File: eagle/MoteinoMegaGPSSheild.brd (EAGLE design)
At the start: 58.1 x 33.6 mm, 26 parts, among them J1 BilgeSwitch, J10 LIPO_VCC, J11 LIPO_GND, J2 Button, J3 LED, J4 DS18B20, J5 DS18B20, J6 5V_GND, J7 OKI-78SR-5/1.5, J8 5V, J9 12-24V_VCC, Q1 NDP6020P, Q2 IRF9Z14PBF, Q3 2N7000

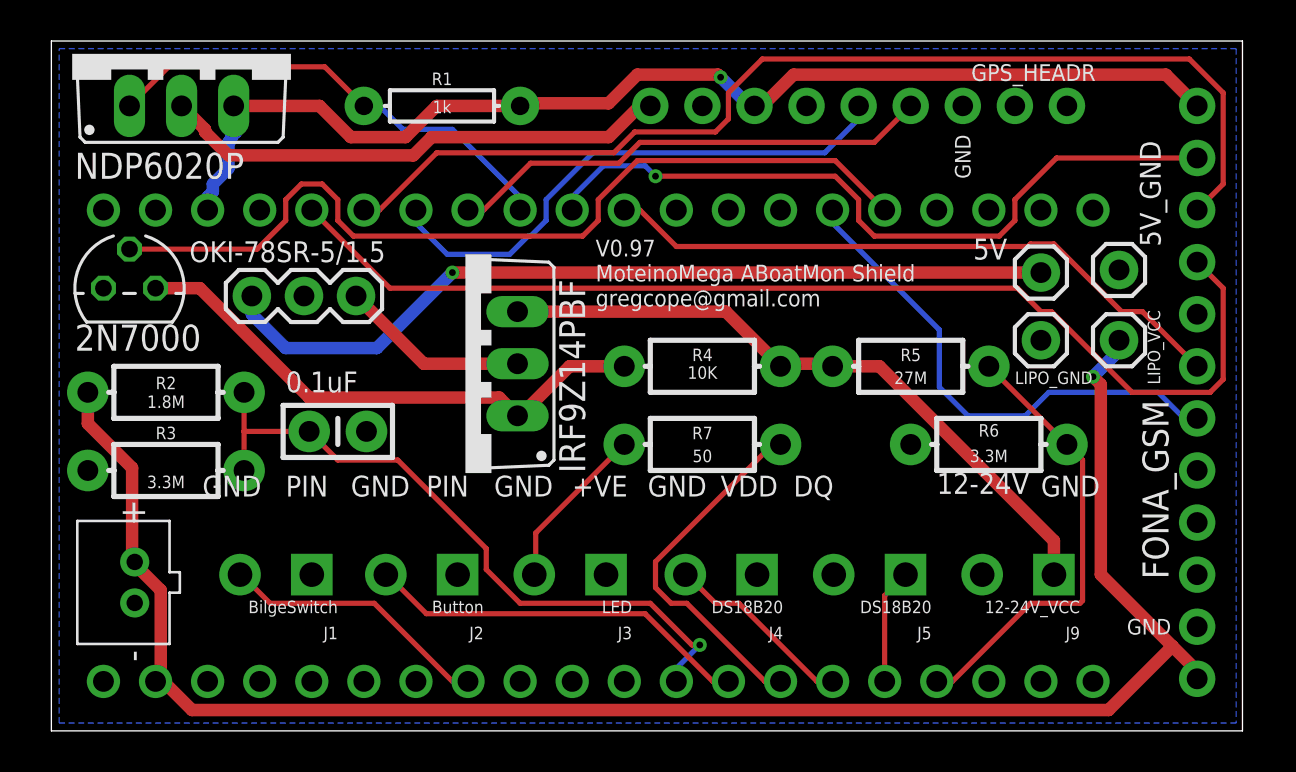
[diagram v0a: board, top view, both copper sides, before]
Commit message: V0.98, schematic layout tweaks, corrected GSM power error, removed GSM power
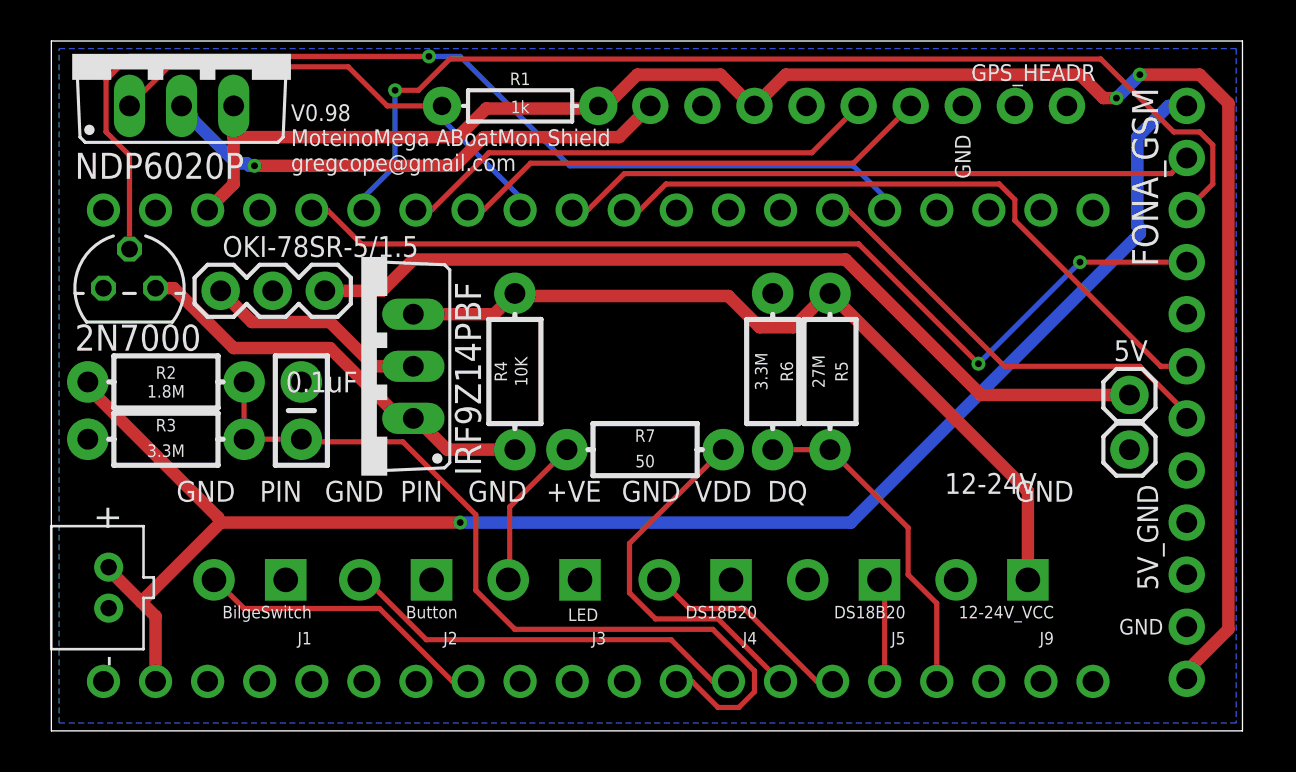
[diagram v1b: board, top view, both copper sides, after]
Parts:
- removed J10: LIPO_VCC, SparkFun-Connectors:1X01
- removed J11: LIPO_GND, SparkFun-Connectors:1X01
- moved R6 11.1 mm to (35.2, 46.7), turned to 270 degrees
- moved R4 9.15 mm to (22.6, 46.7), turned to 90 degrees
- moved J6 8.78 mm to (52.6, 42.9)
- moved J8 7.37 mm to (52.6, 45.6)
- moved Q2 5.08 mm to (15.1, 47.0)
- moved R5 3.95 mm to (38.0, 46.7), turned to 270 degrees
- moved R1 3.81 mm to (22.9, 59.7)
- moved J7 3.57 mm to (13.3, 50.7), turned to 180 degrees
- moved R7 2.81 mm to (29.0, 42.9)
- moved C1 2.05 mm to (12.2, 44.8), turned to 90 degrees
- moved R3 1.52 mm to (5.59, 43.4)
- moved J4 1.30 mm to (33.1, 36.6)
- moved J9 1.30 mm to (47.6, 36.6)
- moved JST1 1.30 mm to (2.79, 36.2)
- moved J1 1.30 mm to (11.4, 36.6)
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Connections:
- net 3.3V: now also JP2.12; no longer JP2.1
- net GND: no longer J11.1
- net VIN: now also JP2.1; no longer J10.1, JP2.12
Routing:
- net 3.3V: track 56.5 -> 87.0 mm, vias 1 -> 2
- net 12-24V-VCC: track 32.5 -> 40.0 mm
- net D19_PWRON: track 43.5 -> 50.7 mm, vias 0 -> 1
- net A0: track 33.2 -> 40.2 mm, vias 1 -> 0
- net D8: track 54.6 -> 47.8 mm, vias 0 -> 2
- net VIN: track 86.3 -> 80.0 mm
- net A5: track 22.1 -> 16.3 mm
- net N$2: track 26.4 -> 20.8 mm
- net D13_NETSTAT: track 35.9 -> 31.0 mm, vias 1 -> 0
- net D18_PS: track 24.9 -> 21.6 mm
- net D10_RX1: track 26.8 -> 23.7 mm
- net 12-24V-SW: track 9.24 -> 10.9 mm
- net D27: track 9.34 -> 10.5 mm
- net D25: track 18.9 -> 20.0 mm
- net D3: track 13.3 -> 14.4 mm
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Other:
- board text added: "V0.98 MoteinoMega ABoatMon Shield gregcope@gmail.com"
- board text removed: "V0.97 MoteinoMega ABoatMon Shield gregcope@gmail.com"

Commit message: Added reverse polarity protection and fuse, as well as GSM FET
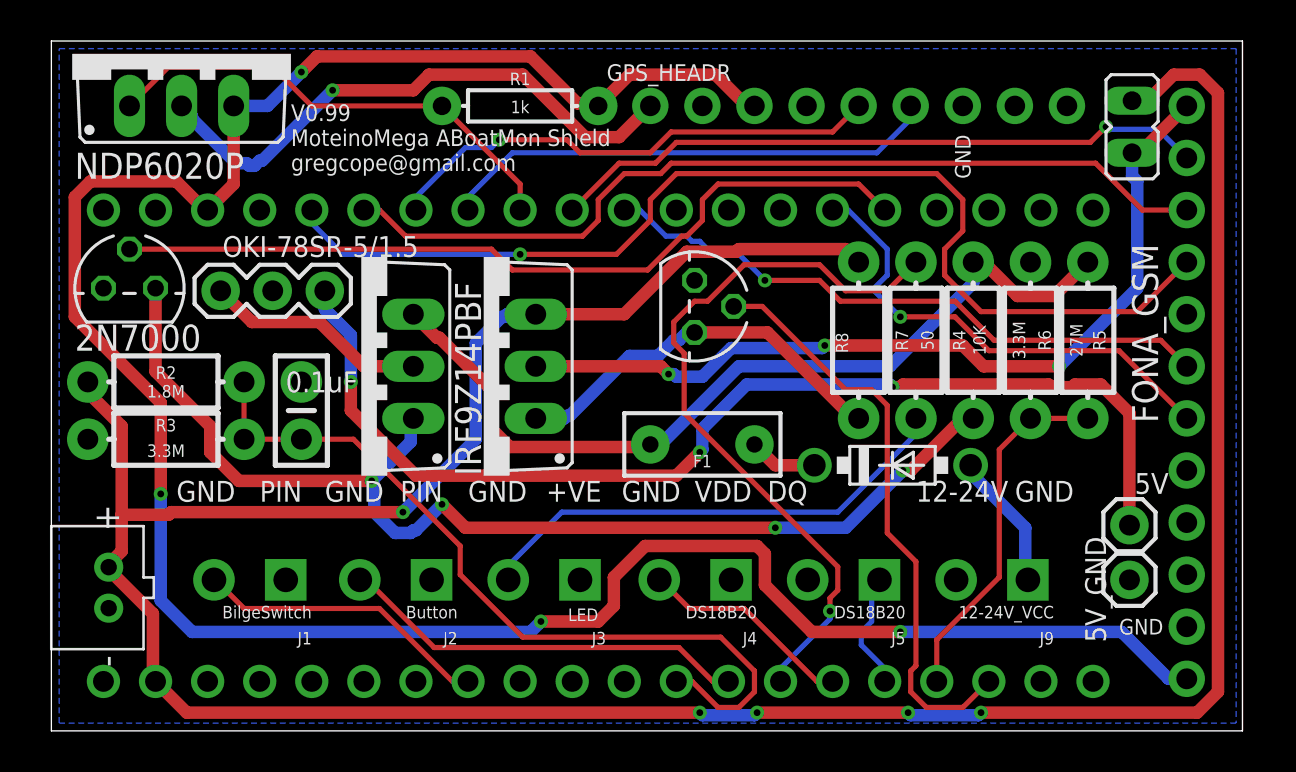
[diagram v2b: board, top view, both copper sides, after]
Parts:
- added D1: 1N5819-B, diode:DO41-7.6
- added F1: 72V/0.25A, SparkFun-Fuses:PTH
- added JP3: VCC_Bypass, jumper:JP1
- added Q4: IRF9Z14PBF, transistor-power:TO220BV
- added Q5: 2N7000, transistors:TO-92
- added R8: 10K, SparkFun-Resistors:AXIAL-0.3-KIT
- moved R4 22.4 mm to (45.0, 48.3)
- moved R7 14.2 mm to (42.2, 48.3), turned to 90 degrees
- moved R5 12.7 mm to (50.5, 48.3)
- moved R6 12.7 mm to (47.8, 48.3)
- moved J6 6.35 mm to (52.6, 36.6)
- moved J8 6.35 mm to (52.6, 39.2)
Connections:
- new net A6: MOTEINO_MEGA.A6, Q5.2
- new net JUMPER: JP2.1, JP3.2, Q4.D
- new net N$5: Q4.G, Q5.3, R8.P$1
- new net N$6: D1.A, J9.1
- new net N$8: D1.C, F1.P$1
- net 12-24V-VCC: now also F1.P$2; no longer J9.1
- net GND: now also Q5.1
- net VIN: now also JP3.1, Q4.S, R8.P$2; no longer JP2.1
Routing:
- net VIN: track 80.0 -> 148.1 mm, vias 1 -> 5
- net JUMPER: track 0.00 -> 42.5 mm, vias 0 -> 3
- net N$2: track 20.8 -> 55.9 mm, vias 0 -> 4
- net 3.3V: track 87.0 -> 119.8 mm, vias 2 -> 4
- net A6: track 0.00 -> 28.8 mm
- net N$5: track 0.00 -> 19.2 mm
- net D26: track 18.0 -> 36.1 mm, vias 0 -> 1
- net N$7: track 7.58 -> 24.0 mm
- net 5V_VCC: track 42.6 -> 54.3 mm, vias 0 -> 3
- net D19_PWRON: track 50.7 -> 40.1 mm, vias 1 -> 0
- net D9: track 52.4 -> 43.7 mm, vias 1 -> 0
- net N$6: track 0.00 -> 6.75 mm
- net D8: track 47.8 -> 53.4 mm, vias 2 -> 1
- net N$8: track 0.00 -> 3.34 mm
- net GPS_VCC: track 25.4 -> 27.9 mm
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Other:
- board text added: "V0.99 MoteinoMega ABoatMon Shield gregcope@gmail.com"
- board text removed: "V0.98 MoteinoMega ABoatMon Shield gregcope@gmail.com"

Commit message: Moved things around, changed P-fets
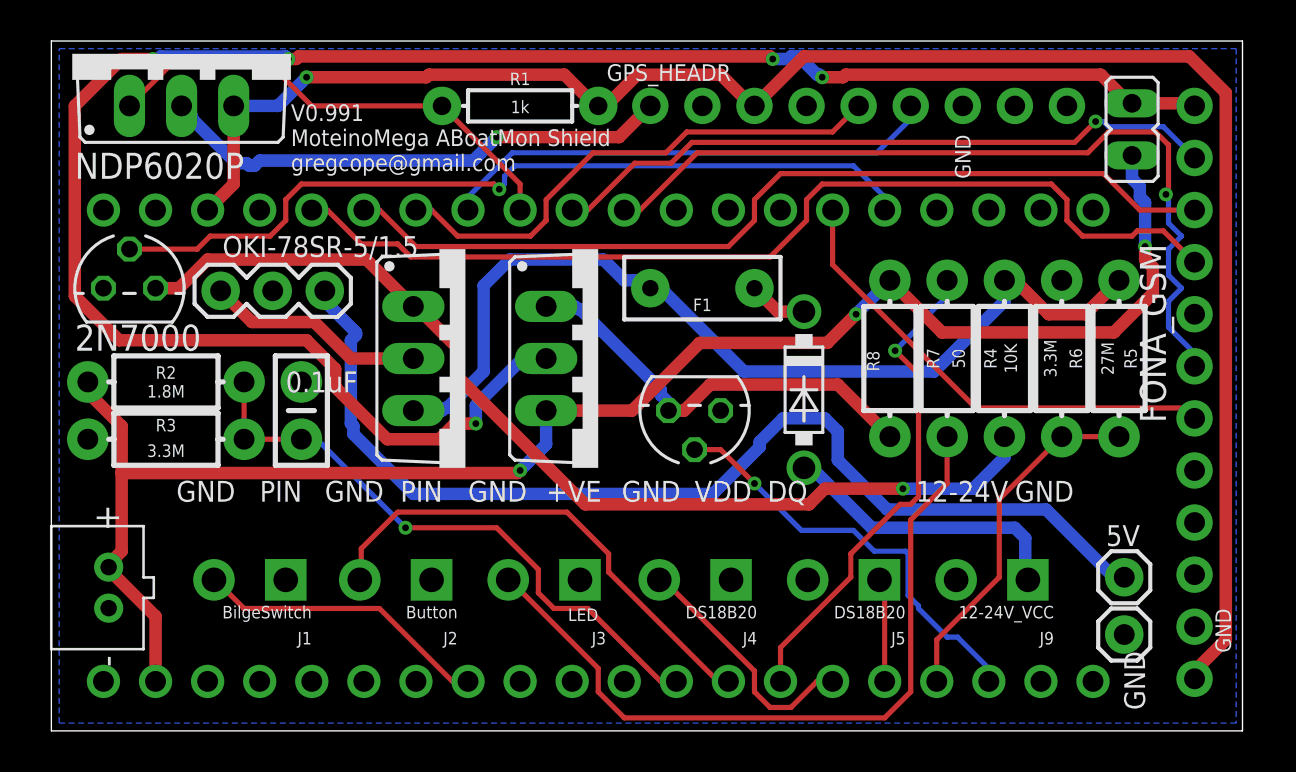
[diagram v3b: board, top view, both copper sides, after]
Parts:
- J6: value 5V_GND -> GND
- moved F1 7.62 mm to (31.8, 50.8)
- moved D1 5.68 mm to (36.7, 45.8), turned to 270 degrees
- moved Q4 5.60 mm to (26.7, 47.4), turned to 270 degrees
- moved Q2 5.09 mm to (20.2, 47.4), turned to 270 degrees
- moved Q5 5.08 mm to (31.4, 44.8), turned to 180 degrees
- moved J6 2.68 mm to (52.3, 33.9)
- moved J8 2.55 mm to (52.3, 36.7)
- moved R4 1.76 mm to (46.5, 47.4)
- moved R5 1.76 mm to (52.1, 47.4)
- moved R6 1.76 mm to (49.3, 47.4)
- moved R7 1.76 mm to (43.7, 47.4)
- moved R8 1.76 mm to (40.9, 47.4)
- moved JP2 0.38 mm to (55.8, 45.7)
- moved JP3 0.13 mm to (52.7, 58.5), turned to 0 degrees
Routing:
- net VIN: track 148.1 -> 80.6 mm, vias 5 -> 3
- net JUMPER: track 42.5 -> 94.7 mm, vias 3 -> 5
- net 3.3V: track 119.8 -> 87.4 mm, vias 4 -> 1
- net N$7: track 24.0 -> 36.8 mm
- net D26: track 36.1 -> 24.2 mm
- net D14_KEY: track 30.6 -> 40.9 mm
- net A0: track 38.9 -> 29.4 mm, vias 0 -> 1
- net A6: track 28.8 -> 20.7 mm, vias 0 -> 1
- net N$6: track 6.75 -> 14.3 mm
- net N$2: track 55.9 -> 49.7 mm, vias 4 -> 1
- net D8: track 53.4 -> 48.5 mm, vias 1 -> 0
- net D25: track 20.0 -> 24.2 mm
- net 12-24V-VCC: track 42.4 -> 46.0 mm
- net GPS_VCC: track 27.9 -> 25.4 mm
- net 5V_VCC: track 54.3 -> 52.3 mm, vias 3 -> 0
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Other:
- board text added: "V0.991 MoteinoMega ABoatMon Shield gregcope@gmail.com"
- board text removed: "V0.99 MoteinoMega ABoatMon Shield gregcope@gmail.com"

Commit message: Changed Resistor shapes
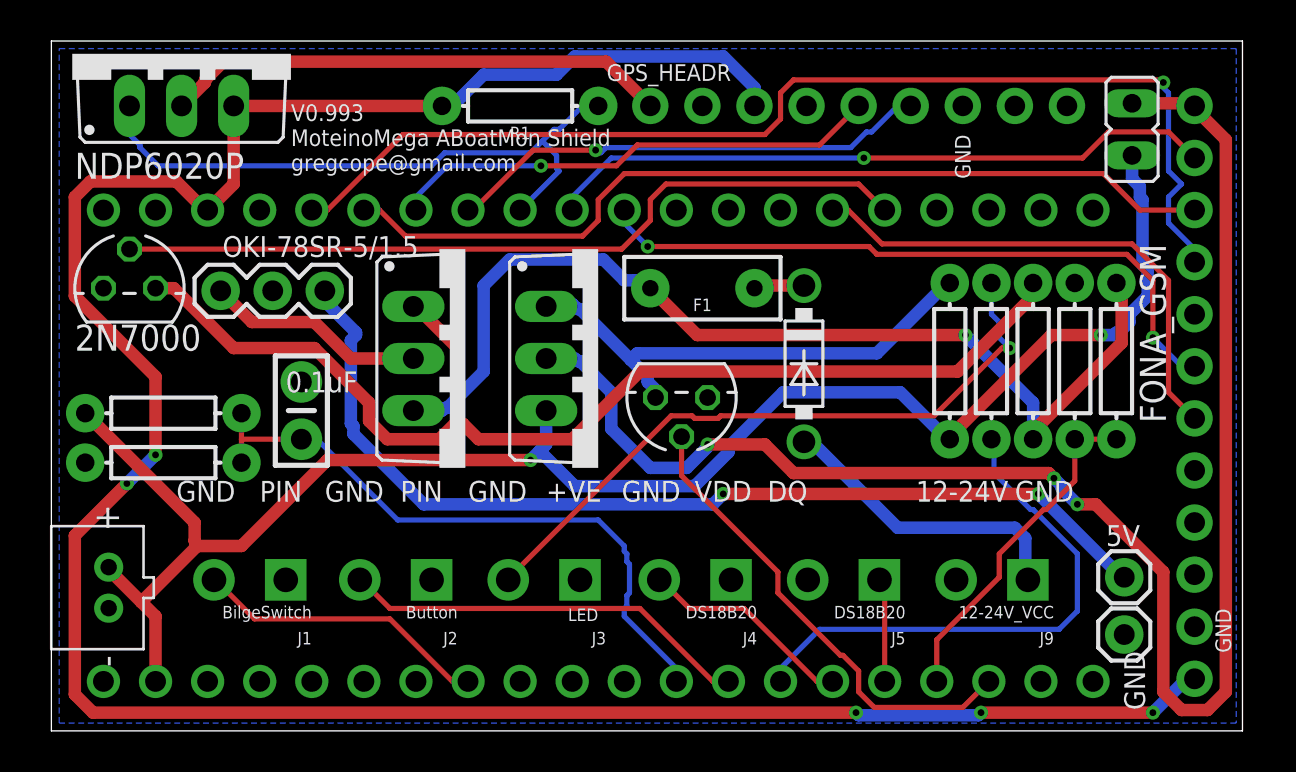
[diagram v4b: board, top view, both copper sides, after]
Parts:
- R2, R3, R4, R5, R6, R7: device SparkFun-Resistors:AXIAL-0.3-KIT -> SparkFun-Resistors:AXIAL-0.3
- R8: value 10K -> 10k; device SparkFun-Resistors:AXIAL-0.3-KIT -> SparkFun-Resistors:AXIAL-0.3
- moved R8 2.92 mm to (43.8, 47.2), turned to 270 degrees
- moved R7 2.16 mm to (45.8, 47.2), turned to 270 degrees
- moved R2 1.53 mm to (5.46, 44.7)
- moved R4 1.40 mm to (47.9, 47.2), turned to 270 degrees
- moved D1 1.27 mm to (36.7, 47.1)
- moved R3 1.15 mm to (5.46, 42.3)
- moved Q5 0.90 mm to (30.7, 45.5)
- moved R6 0.65 mm to (49.9, 47.2)
- moved R5 0.18 mm to (51.9, 47.2), turned to 90 degrees
- turned R1 to 180 degrees
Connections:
- net 12-24V-VCC: now also R5.P$2; no longer R5.P$1
- net A5: now also R5.P$1; no longer R5.P$2
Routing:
- net 3.3V: track 87.4 -> 124.2 mm, vias 1 -> 5
- net JUMPER: track 94.7 -> 78.5 mm, vias 5 -> 3
- net D14_KEY: track 40.9 -> 33.0 mm, vias 1 -> 2
- net N$2: track 49.7 -> 57.2 mm, vias 1 -> 0
- net D12: track 23.5 -> 30.7 mm
- net D8: track 48.5 -> 55.0 mm, vias 0 -> 1
- net D25: track 24.2 -> 20.0 mm
- net 12-24V-VCC: track 46.0 -> 49.9 mm, vias 0 -> 1
- net N$5: track 20.8 -> 24.8 mm
- net N$7: track 36.8 -> 32.9 mm, vias 0 -> 1
- net 5V_VCC: track 52.3 -> 48.7 mm, vias 0 -> 2
- net VIN: track 80.6 -> 83.5 mm, vias 3 -> 2
- net A6: track 20.7 -> 23.3 mm, vias 1 -> 0
- net D26: track 24.2 -> 26.5 mm, vias 1 -> 0
- net A0: track 29.4 -> 31.1 mm, vias 1 -> 0
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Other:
- board text added: "V0.993 MoteinoMega ABoatMon Shield gregcope@gmail.com"
- board text removed: "V0.991 MoteinoMega ABoatMon Shield gregcope@gmail.com"

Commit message: Added current limiting resistors
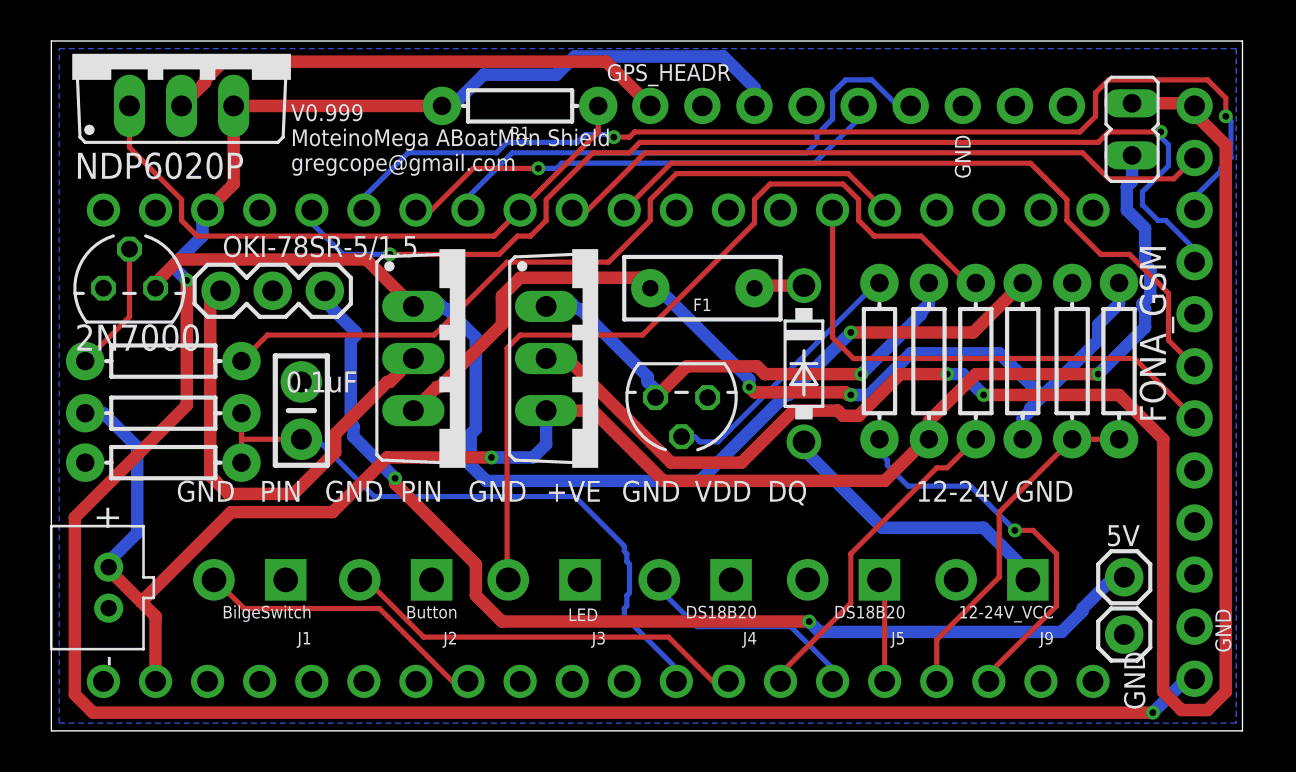
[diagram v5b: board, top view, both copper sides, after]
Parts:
- added R10: 10k, SparkFun-Resistors:AXIAL-0.3
- added R9: 10K, SparkFun-Resistors:AXIAL-0.3
- moved R8 1.02 mm to (42.8, 47.2)
- moved R7 0.76 mm to (45.1, 47.2)
- moved R4 0.51 mm to (47.4, 47.2)
- moved R5 0.13 mm to (52.1, 47.2)
- moved R6 0.13 mm to (49.8, 47.2)
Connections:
- removed net A6: MOTEINO_MEGA.A6, Q5.2
- new net D30: MOTEINO_MEGA.A6, R10.P$1
- new net N$10: Q5.2, R10.P$2
- new net N$9: Q3.2, R9.P$2
- net D19_PWRON: now also R9.P$1; no longer Q3.2
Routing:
- net A6: track 23.3 -> 0.00 mm
- net D30: track 0.00 -> 19.1 mm, vias 0 -> 1
- net N$10: track 0.00 -> 13.0 mm
- net 12-24V-SW: track 10.8 -> 22.8 mm
- net D26: track 26.5 -> 16.1 mm
- net D9: track 43.6 -> 52.5 mm, vias 0 -> 2
- net 3.3V: track 124.2 -> 116.0 mm, vias 5 -> 2
- net N$7: track 32.9 -> 40.8 mm, vias 1 -> 0
- net N$9: track 0.00 -> 6.36 mm
- net JUMPER: track 78.5 -> 84.0 mm, vias 3 -> 2
- net 5V_VCC: track 48.7 -> 51.7 mm
- net D19_PWRON: track 39.3 -> 36.5 mm
- net D11_TX1: track 23.8 -> 26.1 mm, vias 1 -> 0
- net 12-24V-VCC: track 49.9 -> 48.0 mm, vias 1 -> 2
- net D14_KEY: track 33.0 -> 34.8 mm, vias 2 -> 0
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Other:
- board text added: "V0.999 MoteinoMega ABoatMon Shield gregcope@gmail.com"
- board text removed: "V0.993 MoteinoMega ABoatMon Shield gregcope@gmail.com"

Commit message: Routed 100%, finally
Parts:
- JP2: value FONA_GSM -> FONA GSM
- moved J8 41.8 mm to (12.4, 49.3)
- moved R7 15.7 mm to (30.1, 42.4), turned to 0 degrees
- moved R1 6.14 mm to (16.8, 60.5)
- moved J7 6.07 mm to (7.49, 52.3), turned to 0 degrees
- moved R6 3.06 mm to (52.8, 47.0)
- moved R10 2.93 mm to (43.3, 47.0)
- moved R8 2.68 mm to (40.1, 47.0), turned to 90 degrees
- moved J6 2.62 mm to (53.3, 31.5)
- moved R2 2.54 mm to (5.33, 42.2)
- moved R5 2.43 mm to (49.7, 47.0)
- moved R3 2.29 mm to (5.33, 44.6)
- moved Q4 1.53 mm to (25.1, 47.2)
- moved JP3 1.30 mm to (52.5, 59.8)
- moved Q2 1.28 mm to (18.9, 47.2)
- moved Q3 1.27 mm to (2.79, 50.0)
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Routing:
- net D9: track 52.5 -> 107.9 mm, vias 2 -> 0
- net 5V_VCC: track 51.7 -> 6.22 mm, vias 2 -> 0
- net JUMPER: track 84.0 -> 46.9 mm, vias 2 -> 4
- net 3.3V: track 116.0 -> 81.7 mm, vias 2 -> 4
- net N$7: track 40.8 -> 7.54 mm
- net 12-24V-SW: track 22.8 -> 6.73 mm
- net D10_RX1: track 24.1 -> 34.8 mm, vias 1 -> 0
- net A0: track 31.1 -> 40.5 mm
- net D13_NETSTAT: track 32.5 -> 41.4 mm
- net N$2: track 55.6 -> 62.1 mm, vias 1 -> 2
- net D30: track 19.1 -> 12.6 mm, vias 1 -> 0
- net D12: track 30.6 -> 25.0 mm
- net VIN: track 84.2 -> 78.8 mm
- net D19_PWRON: track 36.5 -> 41.7 mm
- net D26: track 16.1 -> 11.7 mm
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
